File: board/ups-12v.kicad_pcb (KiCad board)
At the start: 2 copper layers, 99.8 x 99.4 mm, 109 parts, among them J1 USB_B, J11 Front Panel, J12 Battery Meter, J13 TEMP, J14 V_in, J2 Balancig, J5 Unused Pins, J7 BAT, J8 Mini Buck Module, Q1 AOD423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

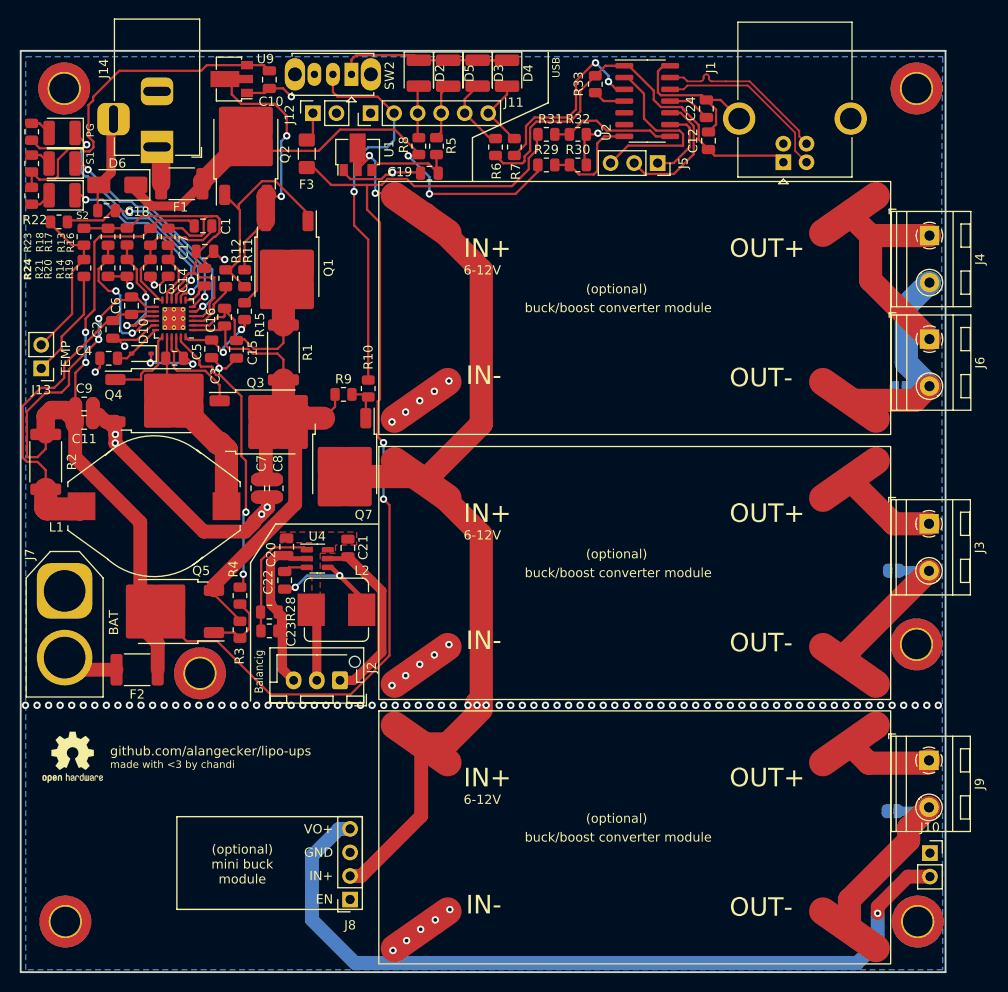
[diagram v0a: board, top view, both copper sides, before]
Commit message: incorporate review feedback
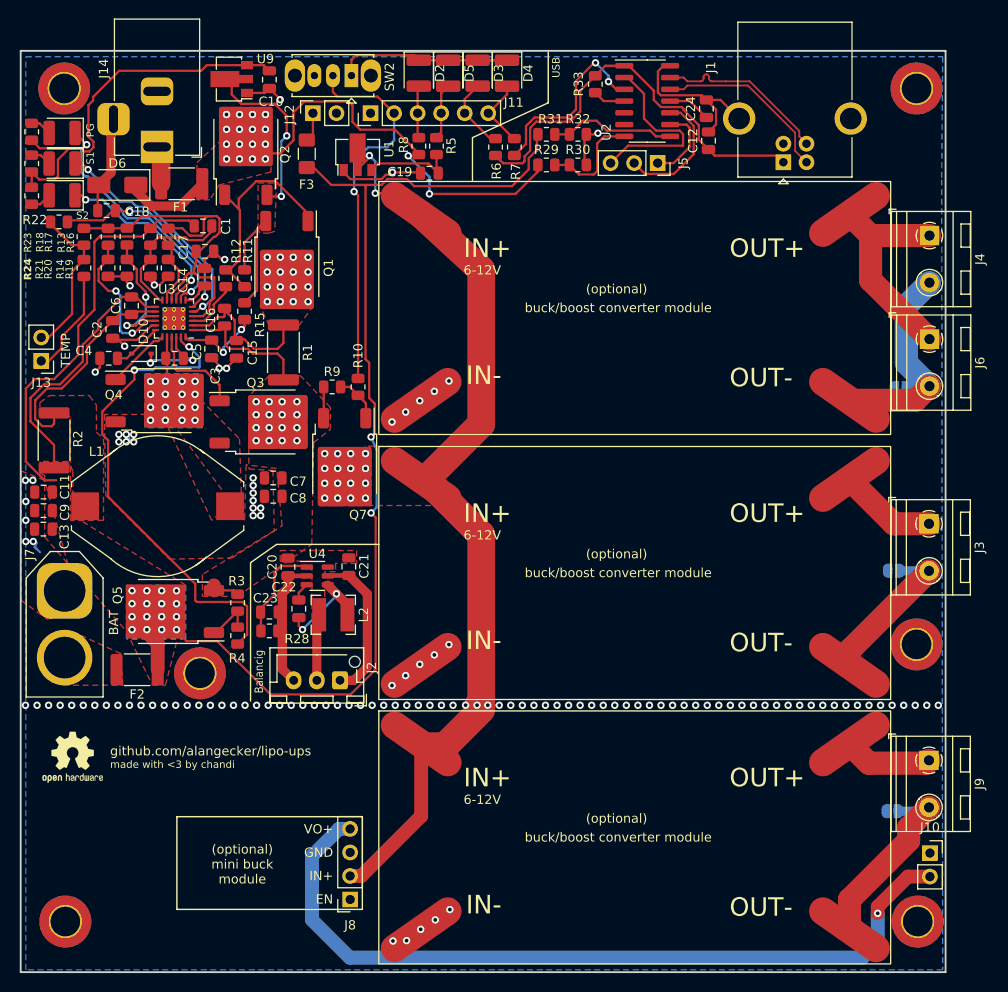
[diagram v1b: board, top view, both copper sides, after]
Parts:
- added C13: DNP, Capacitor_SMD:C_0805_2012Metric, F.Cu at (99.4, 86.5)
- L2: footprint Inductor_SMD:L_Bourns_SRP7028A_7.3x6.6mm -> Inductor_SMD:L_Bourns-SRN4018
- moved C9 12.3 mm to (99.5, 84.5), turned to 180 degrees
- moved C11 8.70 mm to (99.5, 82.5), turned to 180 degrees
- moved R4 4.33 mm to (120.4, 98.0), turned to 90 degrees
- moved C22 3.43 mm to (127.0, 95.2)
- moved R3 2.93 mm to (120.4, 94.5)
- moved R2 2.49 mm to (100.6, 77.0), turned to -90 degrees
- moved C20 2.18 mm to (125.8, 90.6)
- moved C21 2.02 mm to (132.4, 90.6)
- moved C7 2.00 mm to (124.2, 81.0), turned to 180 degrees
- moved U4 1.87 mm to (129.0, 91.6)
- moved R9 1.47 mm to (130.6, 71.2)
- moved R10 1.11 mm to (133.4, 71.2)
- moved C8 0.92 mm to (124.2, 83.0), turned to 180 degrees
- moved J13 0.80 mm to (99.2, 68.4)
- moved L2 0.65 mm to (130.7, 95.8)
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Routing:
- net /charger/SYS: track 58.4 -> 22.4 mm, vias 0 -> 16
- net GND: track 140.4 -> 105.5 mm, vias 36 -> 53
- net Net-(U3-~{BATDRV}): track 31.1 -> 52.2 mm
- net /BAT: track 206.9 -> 188.0 mm, vias 6 -> 18
- net Net-(U3-SRP): track 36.3 -> 23.7 mm
- net Net-(Q3-S): track 18.8 -> 7.19 mm, vias 0 -> 16
- net Net-(J8-Pin_2): track 109.0 -> 103.1 mm, vias 5 -> 22
- net Net-(Q1-D): track 21.5 -> 16.9 mm, vias 0 -> 16
- net Net-(J7-Pin_2): track 6.14 -> 1.85 mm
- net /balancing/BATN: track 20.2 -> 16.1 mm
- net /balancing/BATP: track 19.9 -> 16.5 mm
- net VCC: track 37.6 -> 34.7 mm
- net Net-(U4-ISET): track 13.3 -> 10.8 mm
- net Net-(U4-SW): track 13.3 -> 10.9 mm
- net Net-(Q5-G): track 7.59 -> 5.25 mm
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- added copper zone on B.Cu, net /BAT
- added copper zone on F.Cu, net /BAT
- added copper zone on B.Cu, net /Vin
- added copper zone on F.Cu, net /Vin
- added copper zone on B.Cu, net /charger/SYS
- added copper zone on F.Cu, net /charger/SYS
- added copper zone on F.Cu, net GND
- added copper zone on F.Cu, net Net-(J7-Pin_2)
- added copper zone on B.Cu, net Net-(J8-Pin_2)
- added copper zone on F.Cu, net Net-(J8-Pin_2)
- added copper zone on B.Cu, net Net-(Q1-D)
- added copper zone on F.Cu, net Net-(Q1-D)
- added copper zone on B.Cu, net Net-(Q3-S)
- added copper zone on F.Cu, net Net-(Q3-S)
- added copper zone on F.Cu, net Net-(U3-SRP)
- added copper zone on F.Cu, net VCC
